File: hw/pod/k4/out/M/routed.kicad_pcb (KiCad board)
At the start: 6 copper layers, 15.5 x 12 mm, 37 parts, among them J10 TestPoint_Pad_D1.0mm, J11 TestPoint_Pad_D1.0mm, J20 CONN-SMD_BM28B0.6-30DS-2-0.35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, J3 TestPoint_Pad_D1.0mm, J4 WirePad_1.0x2.0mm, J5 TestPoint_Pad_D1.0mm, J7 TestPoint_Pad_D1.0mm, J8 TestPoint_Pad_D1.0mm, J9 TestPoint_Pad_D1.0mm, SW1 SW-SMD_4P-L3.0-W2.6-P1.85-LS3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, U2 Knowles_LGA-5_3.5x2.65mm, U3 DSBGA-8_L1.6-W0.9-R2-C4-P0.40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, U4 X2SON-4_L1.0-W1.0-P0.65-TL-EP, U6 SOT-553-5_L1.6-W1.2-P0.50-LS1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

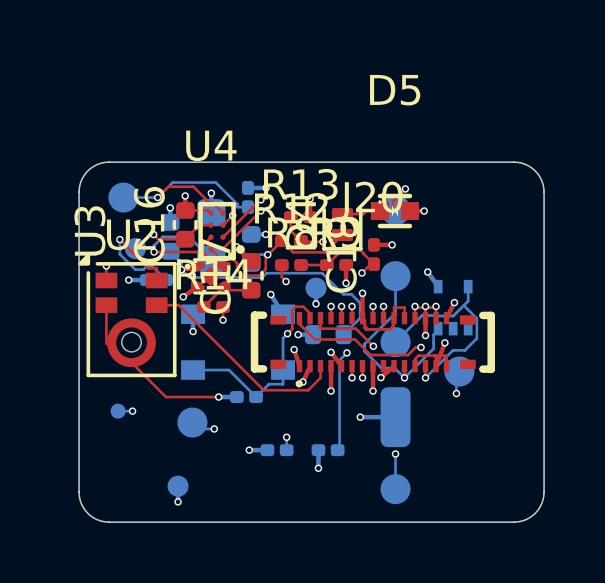
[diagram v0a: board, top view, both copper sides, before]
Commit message: K4 mic-supply filter: R30 33R + C13 on M (MIC_VDDF), k4_noise corrected (P mirror/flip, gap 0.6, JLC 6L stack K4-STACK6): worst-PSRR corner 8.0 dB unfiltered -> 26.4 dB filtered
M re-placed/re-routed (place PASS, 0 unconnected, 0 DRC errors, ERC 0 errors both); P untouched. ECR-0020 rev 5, V9, backlog, vcrm pins, plm 0/0.

Co-Authored-By: Claude Opus 5.5 <noreply@anthropic.com>
Claude-Session: https://claude.ai/code/session_01Wg997D6KFs8bxoAH56jZZJ
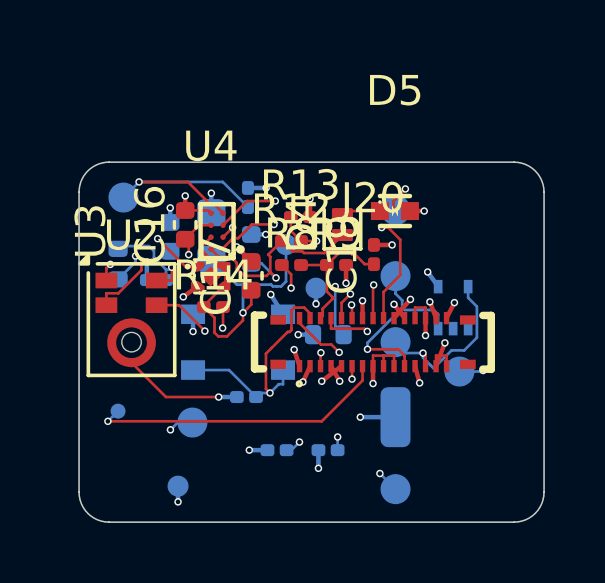
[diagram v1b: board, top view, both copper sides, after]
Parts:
- added R30: R_0402_1005Metric, R_0402_1005Metric, B.Cu at (1.30, 3.40)
- moved TP6 5.02 mm to (6.90, 2.75)
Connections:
- C13 pad 1: MIC_VDD -> MIC_VDDF
- U2 pad 5: MIC_VDD -> MIC_VDDF
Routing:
- net MIC_VDD: track 14.5 -> 10.6 mm
- net VBAT_SENSE: track 8.52 -> 4.87 mm, vias 2 -> 0
- net MIC_VDDF: track 0.00 -> 3.62 mm, vias 0 -> 1
- net TS: track 17.0 -> 20.3 mm
- net VSYS: track 8.98 -> 11.6 mm
- net VBUS_SENSE: track 4.34 -> 6.87 mm
- net I2C_SCL: track 15.6 -> 17.8 mm
- net LDO_OUT: track 9.17 -> 11.1 mm, vias 1 -> 2
- net VBAT: track 16.6 -> 14.9 mm
- net GND: track 28.0 -> 26.4 mm, vias 25 -> 27
- net USB_DM: track 7.41 -> 5.88 mm
- net I2C_SDA: track 12.0 -> 13.3 mm
- net BTN: track 7.04 -> 8.11 mm
- net MIC_DATA: track 15.0 -> 15.9 mm, vias 3 -> 2
- net VBUS: track 6.69 -> 7.50 mm
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
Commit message: K4 lid ledge 0.70 (ECR-0022) + C21 0402: M re-routed 0/0, heights from datasheets: lid +0.112 floor +0.163 worst, B2B gap side still fails (C16 -0.10, C17/C9 -0.05)
Noise F02->MIC_VDD worst corner 28.7 dB, k4_checks PASS, plm 0/0. P untouched.

Co-Authored-By: Claude Opus 5.5 <noreply@anthropic.com>
Claude-Session: https://claude.ai/code/session_01Wg997D6KFs8bxoAH56jZZJ
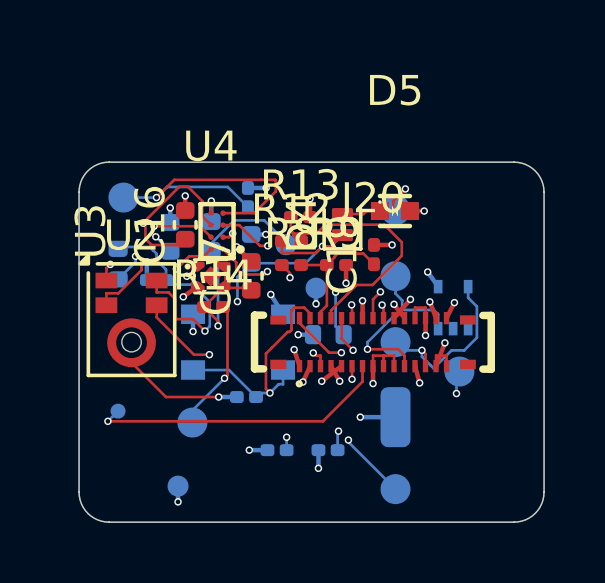
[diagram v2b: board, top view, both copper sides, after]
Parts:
- C21: value C_0603_1608Metric -> C_0402_1005Metric; footprint C_0603_1608Metric -> C_0402_1005Metric
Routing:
- net VBAT: track 14.9 -> 20.8 mm
- net MIC_VDDF: track 3.62 -> 8.14 mm
- net VSYS: track 11.6 -> 15.8 mm, vias 1 -> 2
- net VBUS: track 7.50 -> 10.9 mm, vias 1 -> 3
- net I2C_SDA: track 13.3 -> 10.8 mm
- net CHG_INT: track 6.82 -> 8.93 mm
- net VBUS_SENSE: track 6.87 -> 8.93 mm, vias 2 -> 0
- net I2C_SCL: track 17.8 -> 15.9 mm
- net LDO_OUT: track 11.1 -> 9.63 mm, vias 2 -> 3
- net LED_A: track 5.65 -> 4.39 mm, vias 2 -> 1
- net LED_K: track 7.74 -> 7.14 mm
- net TS: track 20.3 -> 20.9 mm

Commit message: K4 B2B gap: C16/C17 (M) and C9 (P) to Samsung 0201 (0.39 max): gap side 0 fail, worst +0.05 (U3 BQ25180 / D4 0.5 max are package-fixed); D5 0.45, U3 0.5 from datasheets; M re-routed 0/0, P local edit
Co-Authored-By: Claude Opus 5.5 <noreply@anthropic.com>
Claude-Session: https://claude.ai/code/session_01Wg997D6KFs8bxoAH56jZZJ
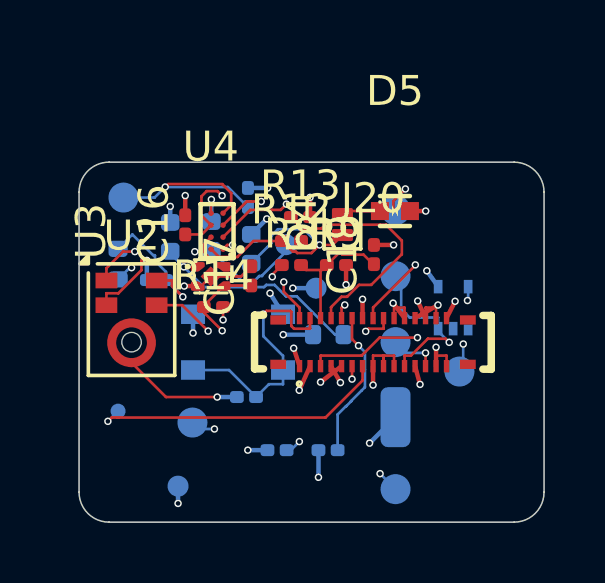
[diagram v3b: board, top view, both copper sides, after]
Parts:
- C16, C17: value C_0402_1005Metric -> C_0201_0603Metric; footprint C_0402_1005Metric -> C_0201_0603Metric
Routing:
- net MIC_CLK: track 6.94 -> 13.7 mm
- net VSYS: track 15.8 -> 11.8 mm
- net VBAT: track 20.8 -> 17.1 mm
- net CHG_INT: track 8.93 -> 5.44 mm
- net MIC_VDDF: track 8.14 -> 4.68 mm
- net TS: track 20.9 -> 17.4 mm
- net GND: track 25.9 -> 29.3 mm, vias 27 -> 25
- net I2C_SCL: track 15.9 -> 19.0 mm
- net LED_K: track 7.14 -> 10.1 mm
- net I2C_SDA: track 10.8 -> 13.6 mm, vias 3 -> 2
- net VBUS: track 10.9 -> 8.23 mm, vias 3 -> 1
- net LDO_OUT: track 9.63 -> 7.50 mm, vias 3 -> 1
- net MIC_DATA: track 15.9 -> 17.6 mm
- net USB_DM: track 6.02 -> 4.39 mm, vias 1 -> 2
- net +3V0: track 5.79 -> 7.34 mm
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
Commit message: K4 re-place/route after 9ec84ae: P and M at L 15.5, plain kicad-cli DRC 0 errors / 0 unconnected both; route_net3d GRID env; pin-contract + ECR-0020 + backlog (C9/C17 datasheet check still open)
Co-Authored-By: Claude Opus 5.5 <noreply@anthropic.com>
Claude-Session: https://claude.ai/code/session_01Wg997D6KFs8bxoAH56jZZJ
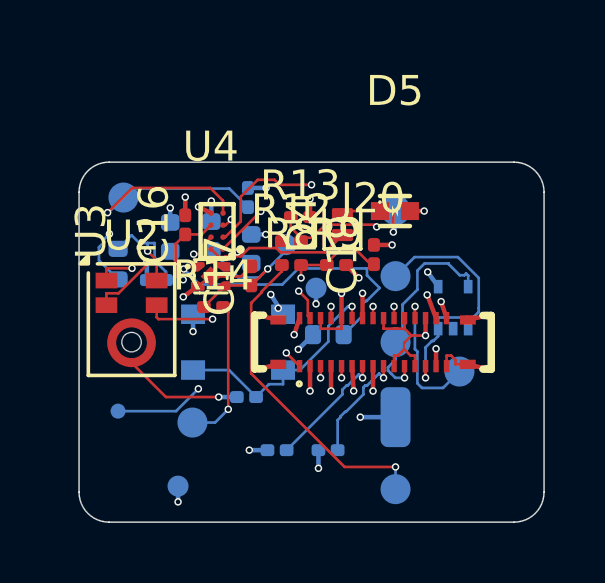
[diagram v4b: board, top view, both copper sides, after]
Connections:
- J20 pad 1: GND -> MIC_VDD
- J20 pad 11: USB_DP -> USB_DM
- J20 pad 13: USB_DM -> USB_DP
- J20 pad 15: GND -> +3V0
- J20 pad 17: +3V0 -> GND
- J20 pad 18: +3V0 -> GND
- J20 pad 19: +3V0 -> LED_K
- J20 pad 21: GND -> MIC_DATA
- J20 pad 22: TS -> GND
- J20 pad 23: I2C_SCL -> CHG_INT
- J20 pad 25: I2C_SDA -> BTN
- J20 pad 26: CHG_INT -> GND
- J20 pad 28: VBAT_SENSE -> GND
- J20 pad 29: BTN -> TS
- J20 pad 30: LED_K -> +3V0
- J20 pad 31: (no net) -> +3V0
- J20 pad 32: (no net) -> +3V0
- J20 pad 33: (no net) -> +3V0
- J20 pad 34: (no net) -> +3V0
- J20 pad 5: GND -> VBAT_SENSE
- J20 pad 6: MIC_VDD -> GND
- J20 pad 7: MIC_DATA -> I2C_SCL
- J20 pad 9: GND -> I2C_SDA
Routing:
- net MIC_CLK: track 13.7 -> 7.09 mm
- net VBAT: track 17.1 -> 23.4 mm, vias 3 -> 2
- net LED_K: track 10.1 -> 4.68 mm, vias 2 -> 1
- net VSYS: track 11.8 -> 8.60 mm
- net LDO_OUT: track 7.50 -> 10.7 mm
- net VBAT_SENSE: track 4.49 -> 7.66 mm, vias 0 -> 2
- net USB_DM: track 4.39 -> 7.16 mm, vias 2 -> 1
- net USB_DP: track 5.74 -> 8.49 mm
- net VBUS: track 8.23 -> 6.02 mm
- net CHG_INT: track 5.44 -> 7.31 mm
- net MIC_DATA: track 17.6 -> 19.1 mm, vias 2 -> 3
- net I2C_SCL: track 19.0 -> 17.6 mm, vias 3 -> 2
- net GND: track 29.3 -> 30.7 mm, vias 25 -> 26
- net TS: track 17.4 -> 18.6 mm
- net VBUS_SENSE: track 8.48 -> 7.39 mm, vias 0 -> 2
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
